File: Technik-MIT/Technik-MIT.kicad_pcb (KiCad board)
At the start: 2 copper layers, 229 x 76.2 mm, 130 parts, among them J1 USB_C_Receptacle_USB2.0, SW1 SW_Push, SW10 SW_Push, SW11 SW_Push, SW12 SW_Push, SW13 SW_Push, SW14 SW_Push, SW15 SW_Push, SW16 SW_Push, SW17 SW_Push, SW18 SW_Push, SW19 SW_Push, SW2 SW_Push, SW20 SW_Push, SW21 SW_Push, SW22 SW_Push, SW23 SW_Push, SW24 SW_Push, SW25 SW_Push, SW26 SW_Push, SW27 SW_Push, SW28 SW_Push, SW29 SW_Push, SW3 SW_Push, SW30 SW_Push, SW31 SW_Push, SW32 SW_Push, SW33 SW_Push, SW34 SW_Push, SW35 SW_Push, SW36 SW_Push, SW37 SW_Push, SW38 SW_Push, SW39 SW_Push, SW4 SW_Push, SW40 SW_Push, SW41 SW_Push, SW42 SW_Push, SW43 SW_Push, SW44 SW_Push, SW45 SW_Push, SW46 SW_Push, SW47 SW_Push, SW5 SW_Push, SW6 SW_Push, SW7 SW_Push, SW8 SW_Push, SW9 SW_Push, U1 USBLC6-2SC6, U2 TVS0500DRV, U3 AP2127N-3.3, U4 W25Q32JVSS, U5 RP2040, Y1 Crystal_GND24

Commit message: Add tooling holes, JLC order number silkscreen.
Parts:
- added H7: MountingHole, Technik-MIT:Tooling Hole, F.Cu at (260.5, 111.5)
- added H8: MountingHole, Technik-MIT:Tooling Hole, F.Cu at (35.5, 42.5)
- added H9: MountingHole, Technik-MIT:Tooling Hole, F.Cu at (35.5, 111.5)
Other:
- board text added: "JLCJLCJLCJLC"
- board text added: "Order Number:"

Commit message: Finalizing PCB layout for print
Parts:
- added C16: 100n, Capacitor_SMD:C_0402_1005Metric, B.Cu at (236.5, 77.9)
- SW40: footprint Technik-MIT:ChocV1_Hotswap -> Technik-MIT:ChocV1_Hotswap_WO_UpperRight
- SW44: footprint Technik-MIT:ChocV1_Hotswap -> Technik-MIT:ChocV1_Hotswap_WO_UpperLeft
- moved U4 19.5 mm to (247.0, 62.8), turned to -90 degrees
- moved R3 18.7 mm to (253.8, 77.2)
- moved BOOTSEL 16.9 mm to (257.3, 81.2)
- moved C3 14.5 mm to (244.1, 68.4), turned to -90 degrees
- moved C14 11.8 mm to (247.6, 83.0), turned to 0 degrees
- moved Y1 8.53 mm to (239.6, 90.9)
- moved C5 8.01 mm to (238.0, 88.7)
- moved C4 3.62 mm to (239.8, 93.1), turned to 0 degrees
- moved D40 3.52 mm to (232.6, 45.2)
- moved D45 3.51 mm to (255.9, 63.3)
- moved D47 3.45 mm to (251.6, 99.3)
- moved D41 3.17 mm to (232.6, 63.3)
- moved D43 3.17 mm to (232.6, 99.3)
- moved U1 1.79 mm to (243.2, 50.0)
- moved C7 1.30 mm to (240.0, 87.8), turned to -90 degrees
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- renumbered RESET to SW48
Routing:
- net /ROW0: track 255.1 -> 282.5 mm, vias 9 -> 7
- net GND: track 7.20 -> 26.2 mm, vias 20 -> 18
- net /ROW1: track 240.9 -> 258.9 mm, vias 7 -> 9
- net /ROW4: track 243.5 -> 259.7 mm, vias 7 -> 8
- net /ROW5: track 220.4 -> 235.3 mm, vias 6 -> 9
- net /QSPI_SD1: track 13.1 -> 27.7 mm, vias 2 -> 0
- net /QSPI_SD2: track 12.7 -> 23.6 mm, vias 2 -> 0
- net Net-(U5-XIN): track 17.9 -> 9.14 mm
- net /QSPI_SS: track 29.1 -> 36.0 mm, vias 2 -> 0
- net /QSPI_SD3: track 22.9 -> 16.2 mm, vias 2 -> 0
- net /QSPI_SCLK: track 21.2 -> 15.7 mm, vias 2 -> 0
- net Net-(C5-Pad2): track 11.2 -> 6.04 mm
- net /ROW6: track 222.5 -> 227.1 mm
- net /ROW7: track 216.4 -> 221.0 mm
- net /ROW3: track 220.3 -> 215.8 mm, vias 6 -> 5
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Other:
- board size 229 x 76.2 mm -> 229 x 76.3 mm
- board text added: "#"
- board text removed: "Order Number:"

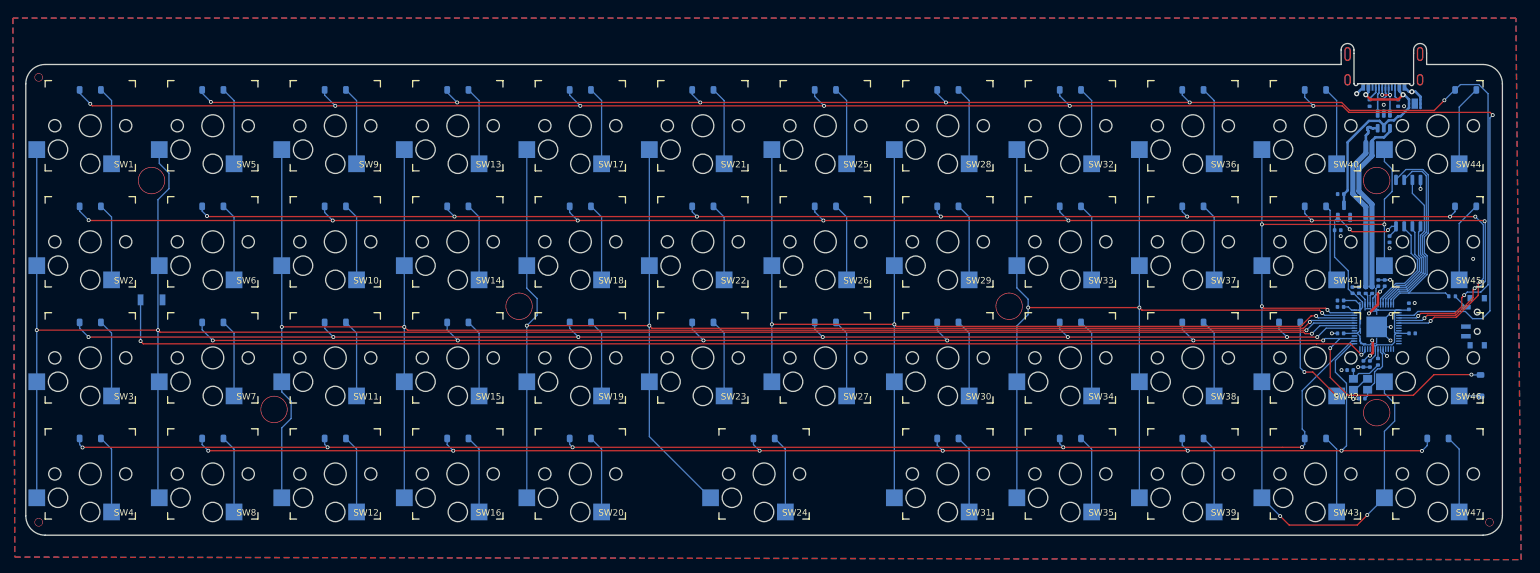
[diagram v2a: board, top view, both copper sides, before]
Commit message: Changed PCB layout & schematics for cheaper production at JLCPCB
Used available basic parts alternatives
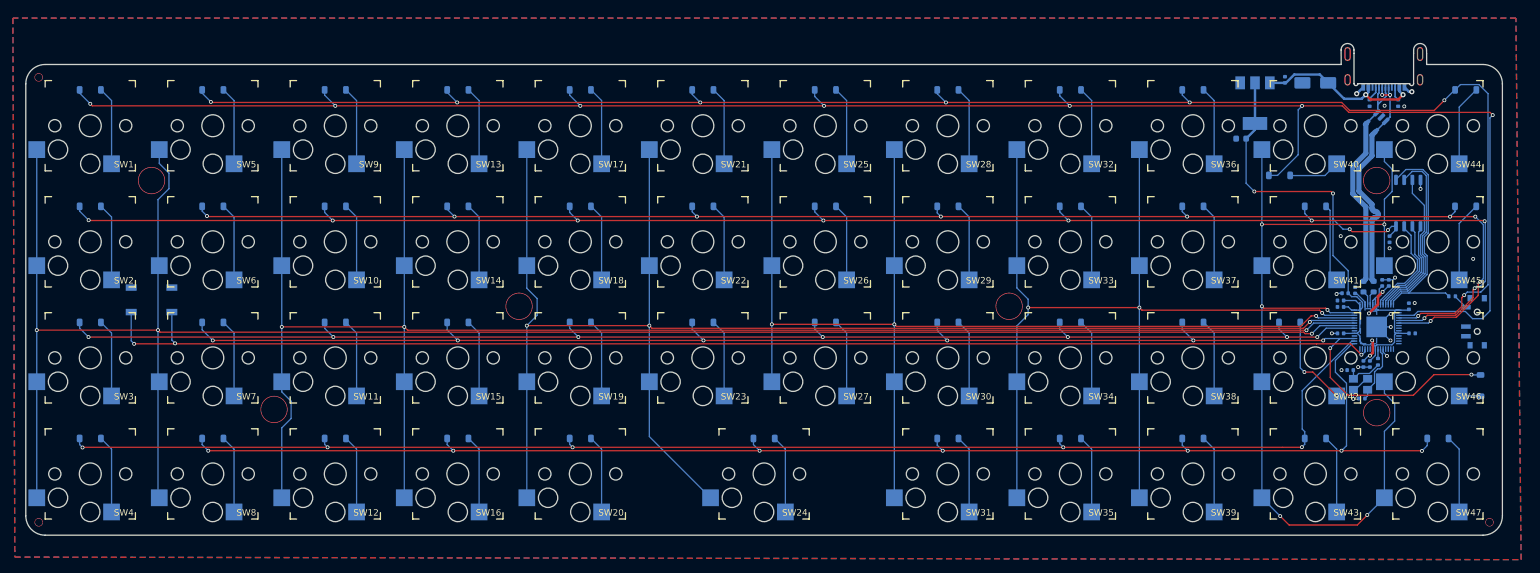
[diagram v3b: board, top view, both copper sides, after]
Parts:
- removed U4: W25Q32JVSS, Package_SO:SOIC-8_5.23x5.23mm_P1.27mm
- added D48: SMAJ5.0A, Diode_SMD:D_SMA, B.Cu at (232.6, 44.1)
- C2: value 1u -> 22u; footprint Capacitor_SMD:C_0402_1005Metric -> Capacitor_SMD:C_0603_1608Metric
- C4, C5: value 27p -> 33p
- R4, R5: footprint Resistor_SMD:R_0402_1005Metric -> Resistor_SMD:R_0603_1608Metric
- RESET: renamed from SW48; footprint Button_Switch_SMD:SW_SPST_B3U-1000P -> Button_Switch_SMD:SW_SPST_TL3342
- U1: value USBLC6-2SC6 -> AMS1117-3.3; footprint Package_TO_SOT_SMD:SOT-23-6 -> Package_TO_SOT_SMD:SOT-223-3_TabPin2
- U2: value TVS0500DRV -> W25Q128JVS; footprint Package_SON:WSON-6-1EP_2x2mm_P0.65mm_EP1x1.6mm -> Package_SO:SOIC-8_5.23x5.23mm_P1.27mm
- U3: value AP2127N-3.3 -> ESDS302; footprint Package_TO_SOT_SMD:SOT-23 -> Package_TO_SOT_SMD:SOT-23-5
- moved C2 20.6 mm to (221.1, 52.8), turned to 180 degrees
- moved U1 20.2 mm to (223.2, 47.3)
- moved C1 19.7 mm to (227.8, 43.7), turned to 90 degrees
- moved U2 15.5 mm to (247.0, 62.8), turned to -90 degrees
- moved U3 14.7 mm to (242.0, 50.2), turned to -135 degrees
- moved D40 14.4 mm to (227.0, 58.5)
- moved C10 1.24 mm to (237.2, 76.8), turned to 180 degrees
- moved R5 0.65 mm to (240.0, 75.8)
- moved C6 0.63 mm to (243.9, 75.2)
- moved C11 0.61 mm to (242.9, 75.2)
- moved R4 0.60 mm to (241.6, 75.8)
- moved C8 0.59 mm to (238.7, 76.3)
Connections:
- J1 pad A6: Net-(J1-D+-PadA6) -> /USB_D+
- J1 pad A7: Net-(J1-D--PadA7) -> /USB_D-
- J1 pad B6: Net-(J1-D+-PadA6) -> /USB_D+
- J1 pad B7: Net-(J1-D--PadA7) -> /USB_D-
- U1 pad 1: Net-(J1-D--PadA7) -> GND
- U1 pad 2: GND -> +3V3
- U1 pad 3: Net-(J1-D+-PadA6) -> VBUS
- U2 pad 1: GND -> /QSPI_SS
- U2 pad 2: GND -> /QSPI_SD1
- U2 pad 3: GND -> /QSPI_SD2
- U2 pad 4: VBUS -> GND
- U2 pad 5: VBUS -> /QSPI_SD0
- U2 pad 6: VBUS -> /QSPI_SCLK
- U2 pad 7: GND -> /QSPI_SD3
- U3 pad 1: GND -> /USB_D-
- U3 pad 2: +3V3 -> GND
- U3 pad 3: VBUS -> /USB_D+
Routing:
- net +3V3: track 71.5 -> 106.3 mm, vias 2 -> 4
- net /ROW0: track 282.5 -> 293.1 mm
- net /USB_D+: track 28.2 -> 36.6 mm, vias 0 -> 2
- net VBUS: track 34.4 -> 26.4 mm
- net /USB_D-: track 28.2 -> 36.0 mm
- net Net-(J1-D--PadA7): track 7.07 -> 0.00 mm
- net Net-(J1-D+-PadA6): track 6.60 -> 0.00 mm, vias 2 -> 0
- net Net-(U5-RUN): track 197.8 -> 202.4 mm, vias 2 -> 3
- net Net-(D40-A): track 12.1 -> 7.99 mm
- net GND: track 26.2 -> 24.0 mm, vias 18 -> 19
- net +1V1: track 15.6 -> 16.3 mm
